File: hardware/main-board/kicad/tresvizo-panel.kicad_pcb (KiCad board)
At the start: 4 copper layers, 50 x 85.5 mm, 128 parts, among them J101 USB_C, J102 BATTERY, J301 GNSS, J401 TF-015, J403 OLED, J404 NTC, Q101 AO3400A, Q102 AO3401A, Q103 AO3400A, Q401 AO3401A, SW201 RESET, SW202 BOOT, SW401 BOTON, U101 USBLC6-2SC6, U102 BQ25798RQMR, U103 MAX17048G+T10, U105 TPS62903RPJR, U201 ESP32-S3-WROOM-1-N16R2, U301 TPS63070RNMR, U302 USBLC6-2SC6, U303 USBLC6-2SC6, U401 BMI088

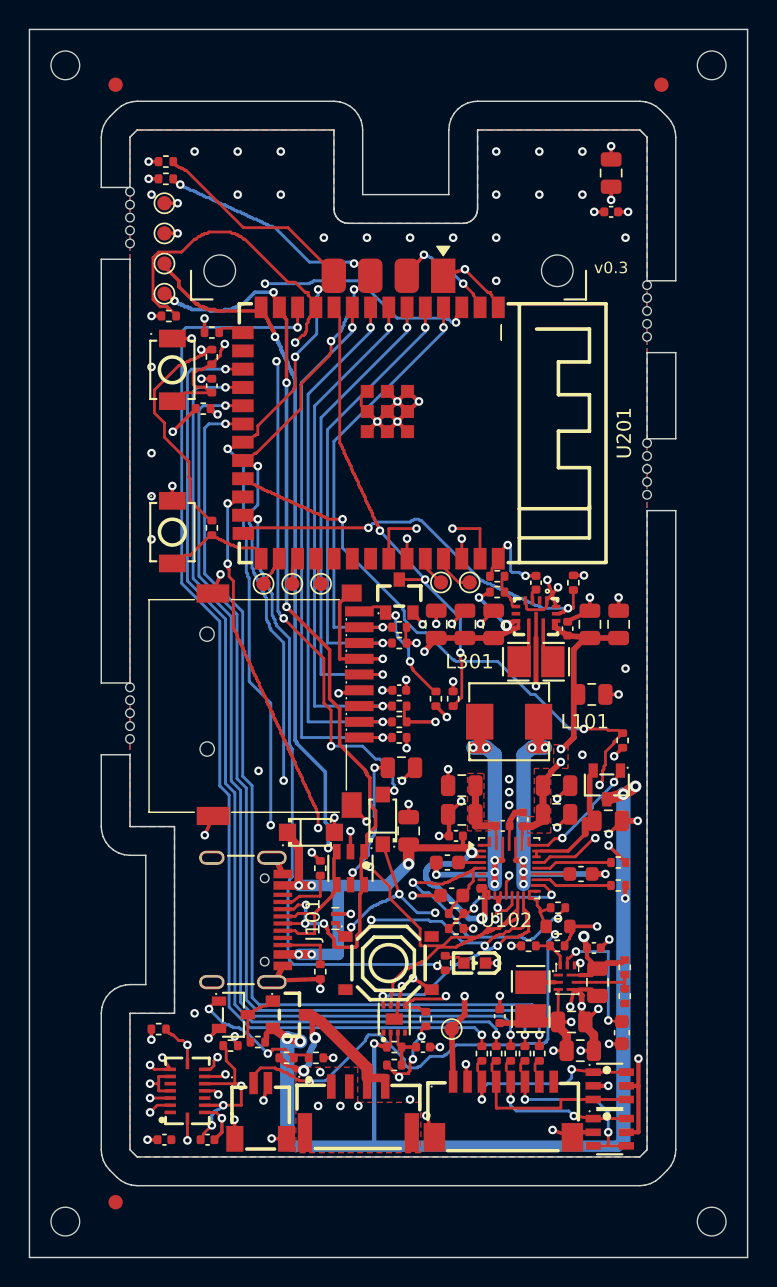
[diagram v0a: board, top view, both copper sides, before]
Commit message: v0.3: OLED con VCC en el pin 1 y microSD en su posición real, con muesca de 8
Placa v0.3:
- J403 pasa a VCC, GND, SCL, SDA, que es lo que dice la foto del anuncio del módulo del
  propietario (Mercado Libre, ANPOMNHBUK). Antes era GND, VCC: la OLED habría recibido la
  alimentación invertida. Antes de pedir hay que confirmarlo en la serigrafía de la unidad.
- El anuncio da el controlador SSD1315, compatible con las bibliotecas del SSD1306: queda en la
  tabla del firmware.
- Placa rehecha con build.py: ERC 0, DRC 0/0/0 y panel 0/0. Cambia el ruteo; la colocación no.
- Plano de LCD wiki de la OLED (MC096) comparado con el del vendedor: coinciden en vidrio,
  agujeros y PCB, y da los espesores (PCB 1.2, vidrio 1.5).

Carcasa V3.0:
- Posición de la tarjeta según la hoja de SOFNG del TF-015 (LCSC C113206), desde la boca de J401:
  trabada asoma 2.50 (x 19.0, antes x 17.5 en el modelo), se empuja hasta 1.32 para soltarla y
  expulsada asoma 5.60. En la muesca, la trabada queda 0.4 bajo la cara de fuera y la expulsada
  sobresale 2.7.
- Muesca para la uña de 5 a 8 mm, para que entre la yema.
- El cuerpo de TPU de la tapa en la ranura empieza en r 26.0: queda a 0.54 del canto de la
  tarjeta trabada, así cerrar la tapa no la empuja (el zócalo es de empuje).
- check_v3_0.py: la tarjeta trabada va en su ranura con el ajuste guiado de 0.3, como la funda
  del USB-C, y no cuenta como aire a piezas compradas.
- Comprobación con el STEP real de la placa: 0 choques en posición final y en los 11 barridos,
  guarda de pared sin faltantes y objetivos B1, B2, B3 y B7 cumplidos.

Pendiente: confirmar el orden de los pines en la OLED real, probar impresa la muesca y la tapa
de puertos, medir el pack, la carrier y los agujeros de la OLED, y confirmar el conector de la
antena.
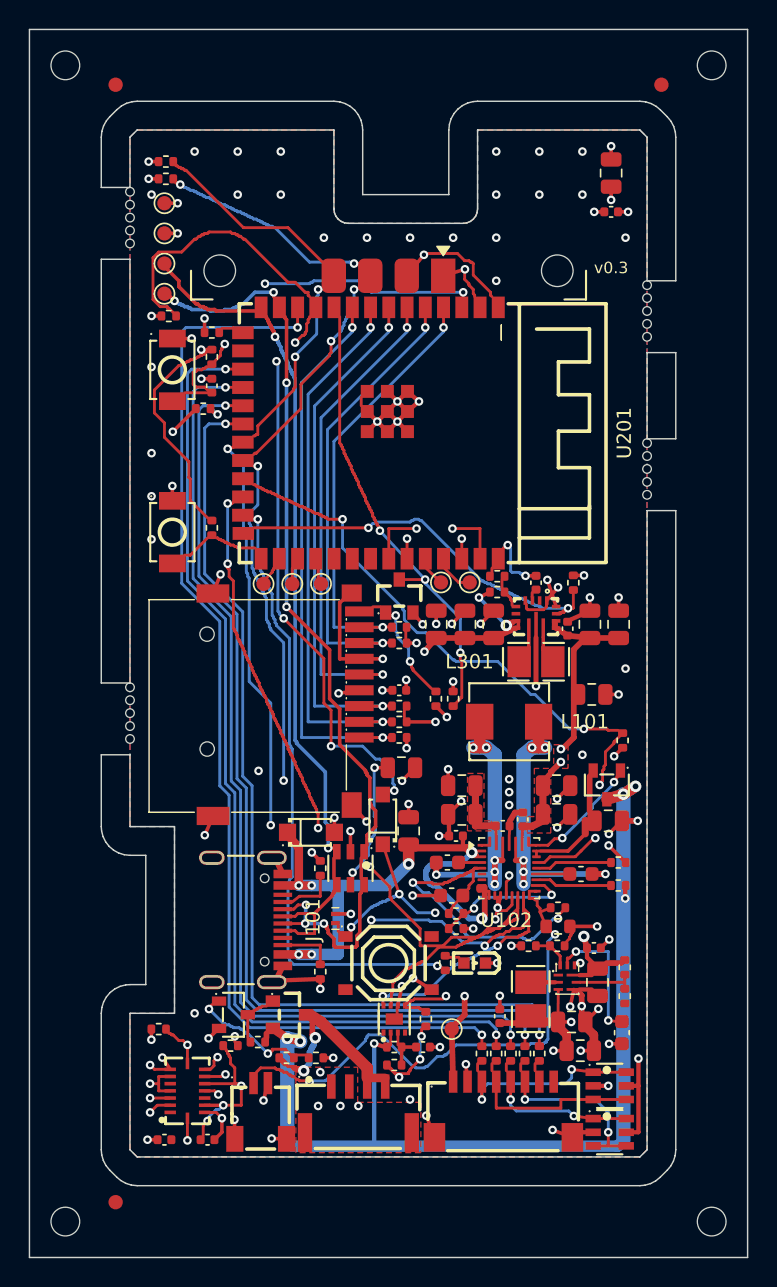
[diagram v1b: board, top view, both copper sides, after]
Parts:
- removed the TH3 at (102.5, 183.0)
- removed the TH4 at (147.5, 183.0)
- added TH1: TH1, , F.Cu at (102.5, 102.5)
- added TH2: TH2, , F.Cu at (147.5, 102.5)
- TH3: renamed from TH1; value TH1 -> TH3
- TH4: renamed from TH2; value TH2 -> TH4
- moved TH3 80.5 mm to (102.5, 183.0)
- moved TH4 80.5 mm to (147.5, 183.0)
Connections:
- J403 pad 1: GND -> +3V3
- J403 pad 2: +3V3 -> GND
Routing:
- net GND: track 134.6 -> 138.7 mm
- net +3V3: track 87.5 -> 83.9 mm, vias 34 -> 33
